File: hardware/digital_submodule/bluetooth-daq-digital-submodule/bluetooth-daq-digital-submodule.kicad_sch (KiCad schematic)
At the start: 163 parts, among them J1 MCU I/F, J2 Digital Inputs, J3 Digital Outputs, J4 Communication I/F, J5 RS-485 I/F, U1 74HC595, U2 74HC595, U3 74HC165, U4 74HC165, U5 24LC1025, U6 SN75176AD, U7 CD4053B, U8 CD4053B

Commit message: Addressed errors raised by KiCAD for digital sub-module.
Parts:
- added R200: 10k, symbol Device:R
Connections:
- net GND: now also R200.1
- net at U5.3 (A2): now also R200.2
- net 3V3 renamed +3V3
- net 5V renamed +5V

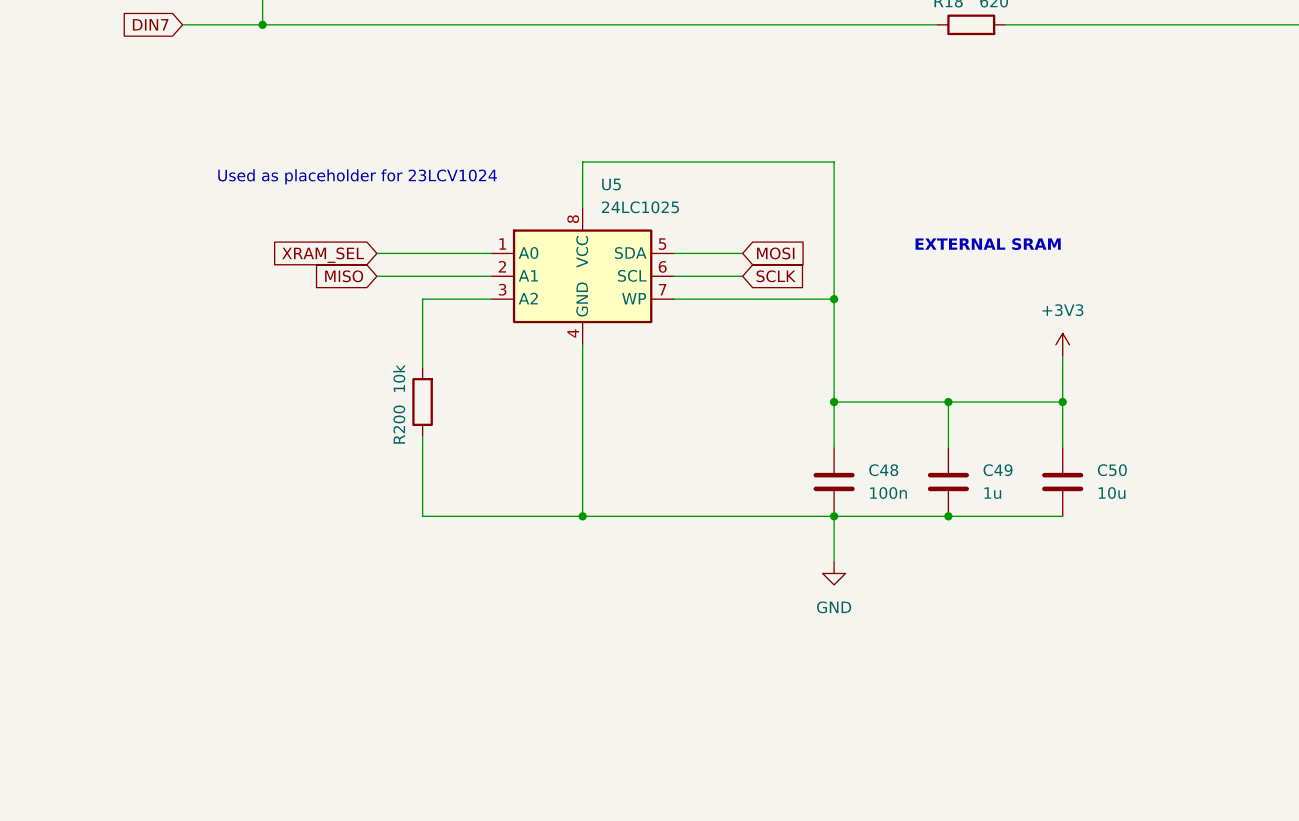
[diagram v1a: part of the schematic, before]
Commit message: Added footprints for components in digital_submodule
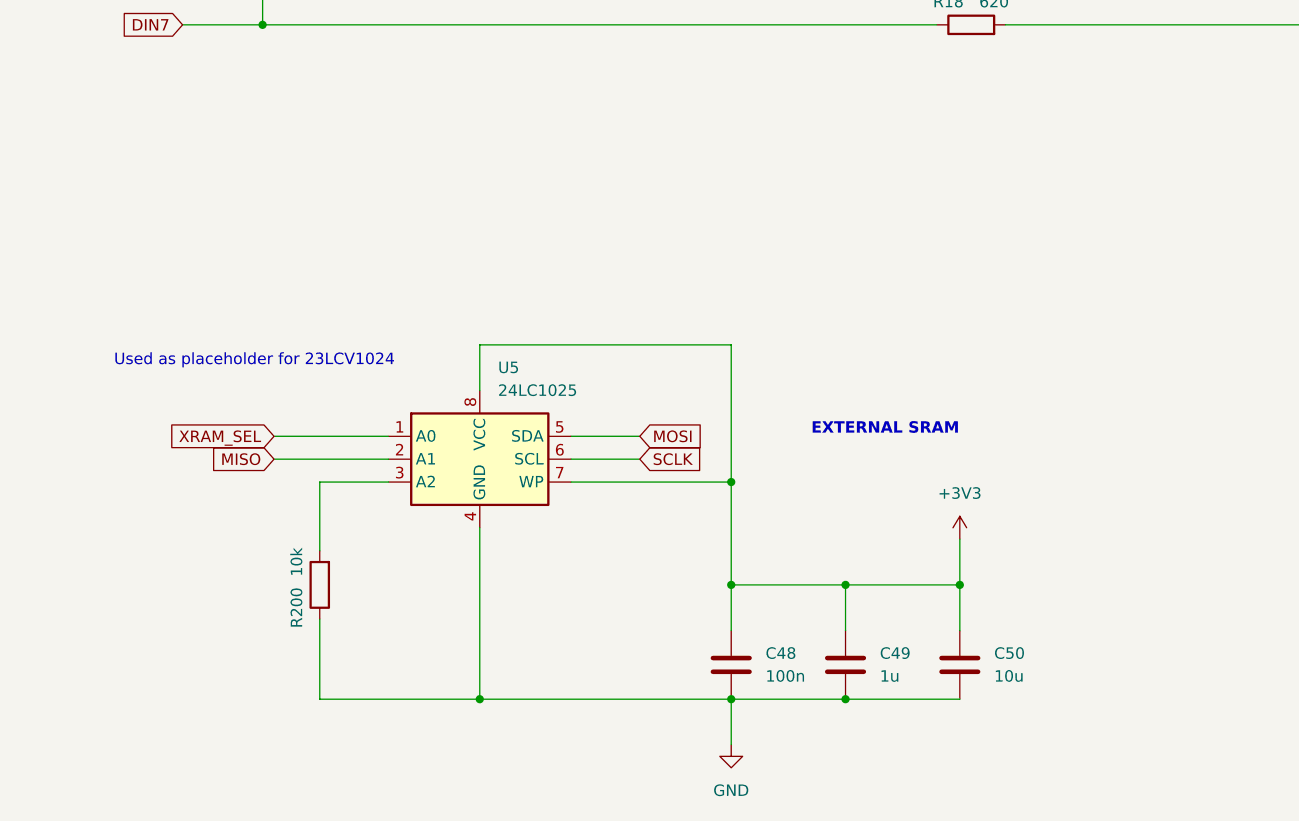
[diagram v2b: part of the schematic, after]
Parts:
- C1, C10, C11, C12, C13, C14, C15, C16, C17, C18, C19, C2, C20, C21, C22, C23, C24, C25, C29, C3, C30, C31, C32, C33, C34, C35, C36, C37, C38, C39, C4, C40, C41, C42, C43, C44, C45, C46, C47, C48, C49, C5, C50, C51, C52, C53, C54, C55, C56, C57, C6, C7, C8, C9: footprint (none) -> Capacitor_SMD:C_0805_2012Metric_Pad1.18x1.45mm_HandSolder
- D1, D10, D11, D12, D13, D14, D15, D16, D17, D18, D19, D2, D20, D21, D22, D23, D24, D25, D26, D27, D28, D29, D3, D30, D31, D32, D33, D34, D35, D36, D37, D38, D39, D4, D5, D6, D7, D8, D9: footprint (none) -> Diode_SMD:D_SMA_Handsoldering
- J1, J2, J3, J4: footprint (none) -> Connector_PinHeader_2.54mm:PinHeader_2x08_P2.54mm_Vertical
- J5: footprint (none) -> Connector_Phoenix_MC_HighVoltage:PhoenixContact_MCV_1,5_2-G-5.08_1x02_P5.08mm_Vertical
- R1, R10, R11, R12, R13, R14, R15, R16, R17, R18, R19, R2, R20, R200, R21, R22, R23, R24, R25, R26, R27, R28, R29, R3, R30, R31, R32, R33, R34, R35, R4, R41, R42, R43, R44, R45, R46, R47, R48, R49, R5, R50, R51, R52, R53, R54, R55, R56, R57, R58, R59, R6, R7, R8, R9: footprint (none) -> Resistor_SMD:R_0805_2012Metric_Pad1.20x1.40mm_HandSolder
- R38, R39, R40: footprint (none) -> Resistor_SMD:R_1206_3216Metric_Pad1.30x1.75mm_HandSolder
- U1, U2: footprint (none) -> Package_SO:SOIC-16_3.9x9.9mm_P1.27mm
- U3, U4: footprint (none) -> SN74HC165_custom:D16
- U5: footprint (none) -> 23LCV1024:SOIC8-N_MC_MCH
- U7, U8: footprint (none) -> CD4053BE_custom:D16
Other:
- moved on the sheet: C48, C49, C50, R200, U5

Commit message: Arranged components in PCB view according their functionality
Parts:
- removed D1, D10, D11, D12, D13, D14, D15, D16, D17, D18, D19, D2, D20, D21, D22, D23, D24, D25, D26, D27, D28, D29, D3, D30, D31, D32, D4, D5, D6, D7, D8, D9: SMAJ5.0CA, Diode_SMD:D_SMA_Handsoldering, symbol Device:D_TVS
- added DIP0, DIP1, DIP10, DIP11, DIP12, DIP13, DIP14, DIP15, DIP2, DIP3, DIP4, DIP5, DIP6, DIP7, DIP8, DIP9: D_Schottky, Diode_SMD:D_SMA_Handsoldering, symbol Device:D_Schottky
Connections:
- net GND: now also DIP0.2 (A), DIP1.2 (A), DIP10.2 (A), DIP11.2 (A), DIP12.2 (A), DIP13.2 (A), DIP14.2 (A), DIP15.2 (A), DIP2.2 (A), DIP3.2 (A), DIP4.2 (A), DIP5.2 (A), DIP6.2 (A), DIP7.2 (A), DIP8.2 (A), DIP9.2 (A)
- net at R23.2, U3.13 (D2): now also DIP2.1 (K)
- net at R21.2, U3.3 (D4): now also DIP4.1 (K)
- net at R34.2, U4.12 (D1): now also DIP9.1 (K)
- net at R18.2, U3.6 (D7): now also DIP7.1 (K)
- net at R22.2, U3.14 (D3): now also DIP3.1 (K)
- net at R25.2, U3.11 (D0): now also DIP0.1 (K)
- net at R24.2, U3.12 (D1): now also DIP1.1 (K)
- net at R20.2, U3.4 (D5): now also DIP5.1 (K)
- net at R19.2, U3.5 (D6): now also DIP6.1 (K)
- net at R33.2, U4.13 (D2): now also DIP10.1 (K)
- net at R30.2, U4.4 (D5): now also DIP13.1 (K)
- net at R35.2, U4.11 (D0): now also DIP8.1 (K)
- net at R28.2, U4.6 (D7): now also DIP15.1 (K)
- net at R32.2, U4.14 (D3): now also DIP11.1 (K)
- net at R29.2, U4.5 (D6): now also DIP14.1 (K)
- net at R31.2, U4.3 (D4): now also DIP12.1 (K)

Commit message: Decided on component arangement for digital input and digital output sections of the digital submodule.
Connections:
- net DIN0: no longer C29.2
- net DIN1: no longer C30.2
- net DIN10: no longer C45.2
- net DIN11: no longer C44.2
- net DIN12: no longer C43.2
- net DIN13: no longer C42.2
- net DIN14: no longer C41.2
- net DIN15: no longer C40.2
- net DIN2: no longer C31.2
- net DIN3: no longer C32.2
- net DIN4: no longer C33.2
- net DIN5: no longer C34.2
- net DIN6: no longer C35.2
- net DIN7: no longer C36.2
- net DIN8: no longer C47.2
- net DIN9: no longer C46.2
- net DOUT0: now also J3.15 (Pin_15); no longer J3.1 (Pin_1)
- net DOUT1: now also J3.13 (Pin_13); no longer J3.3 (Pin_3)
- net DOUT10: now also J3.12 (Pin_12); no longer J3.6 (Pin_6)
- net DOUT11: now also J3.10 (Pin_10); no longer J3.8 (Pin_8)
- net DOUT12: now also J3.8 (Pin_8); no longer J3.10 (Pin_10)
- net DOUT13: now also J3.6 (Pin_6); no longer J3.12 (Pin_12)
- net DOUT14: now also J3.4 (Pin_4); no longer J3.14 (Pin_14)
- net DOUT15: now also J3.2 (Pin_2); no longer J3.16 (Pin_16)
- net DOUT2: now also J3.11 (Pin_11); no longer J3.5 (Pin_5)
- net DOUT3: now also J3.9 (Pin_9); no longer J3.7 (Pin_7)
- net DOUT4: now also J3.7 (Pin_7); no longer J3.9 (Pin_9)
- net DOUT5: now also J3.5 (Pin_5); no longer J3.11 (Pin_11)
- net DOUT6: now also J3.3 (Pin_3); no longer J3.13 (Pin_13)
- net DOUT7: now also J3.1 (Pin_1); no longer J3.15 (Pin_15)
- net DOUT8: now also J3.16 (Pin_16); no longer J3.2 (Pin_2)
- net DOUT9: now also J3.14 (Pin_14); no longer J3.4 (Pin_4)
- net at DIP11.1 (K), R32.2, U4.14 (D3): now also C43.2
- net at DIP2.1 (K), R23.2, U3.13 (D2): now also C34.2
- net at DIP4.1 (K), R21.2, U3.3 (D4): now also C32.2
- net at DIP7.1 (K), R18.2, U3.6 (D7): now also C29.2
- net at DIP5.1 (K), R20.2, U3.4 (D5): now also C31.2
- net at DIP0.1 (K), R25.2, U3.11 (D0): now also C36.2
- net at DIP1.1 (K), R24.2, U3.12 (D1): now also C35.2
- net at DIP3.1 (K), R22.2, U3.14 (D3): now also C33.2
- net at DIP6.1 (K), R19.2, U3.5 (D6): now also C30.2
- net at DIP9.1 (K), R34.2, U4.12 (D1): now also C41.2
- net at DIP13.1 (K), R30.2, U4.4 (D5): now also C45.2
- net at DIP8.1 (K), R35.2, U4.11 (D0): now also C40.2
- net at DIP15.1 (K), R28.2, U4.6 (D7): now also C47.2
- net at DIP14.1 (K), R29.2, U4.5 (D6): now also C46.2
- net at DIP12.1 (K), R31.2, U4.3 (D4): now also C44.2
- net at DIP10.1 (K), R33.2, U4.13 (D2): now also C42.2
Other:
- moved on the sheet: C29, C30, C31, C32, C33, C34, C35, C36, C40, C41, C42, C43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

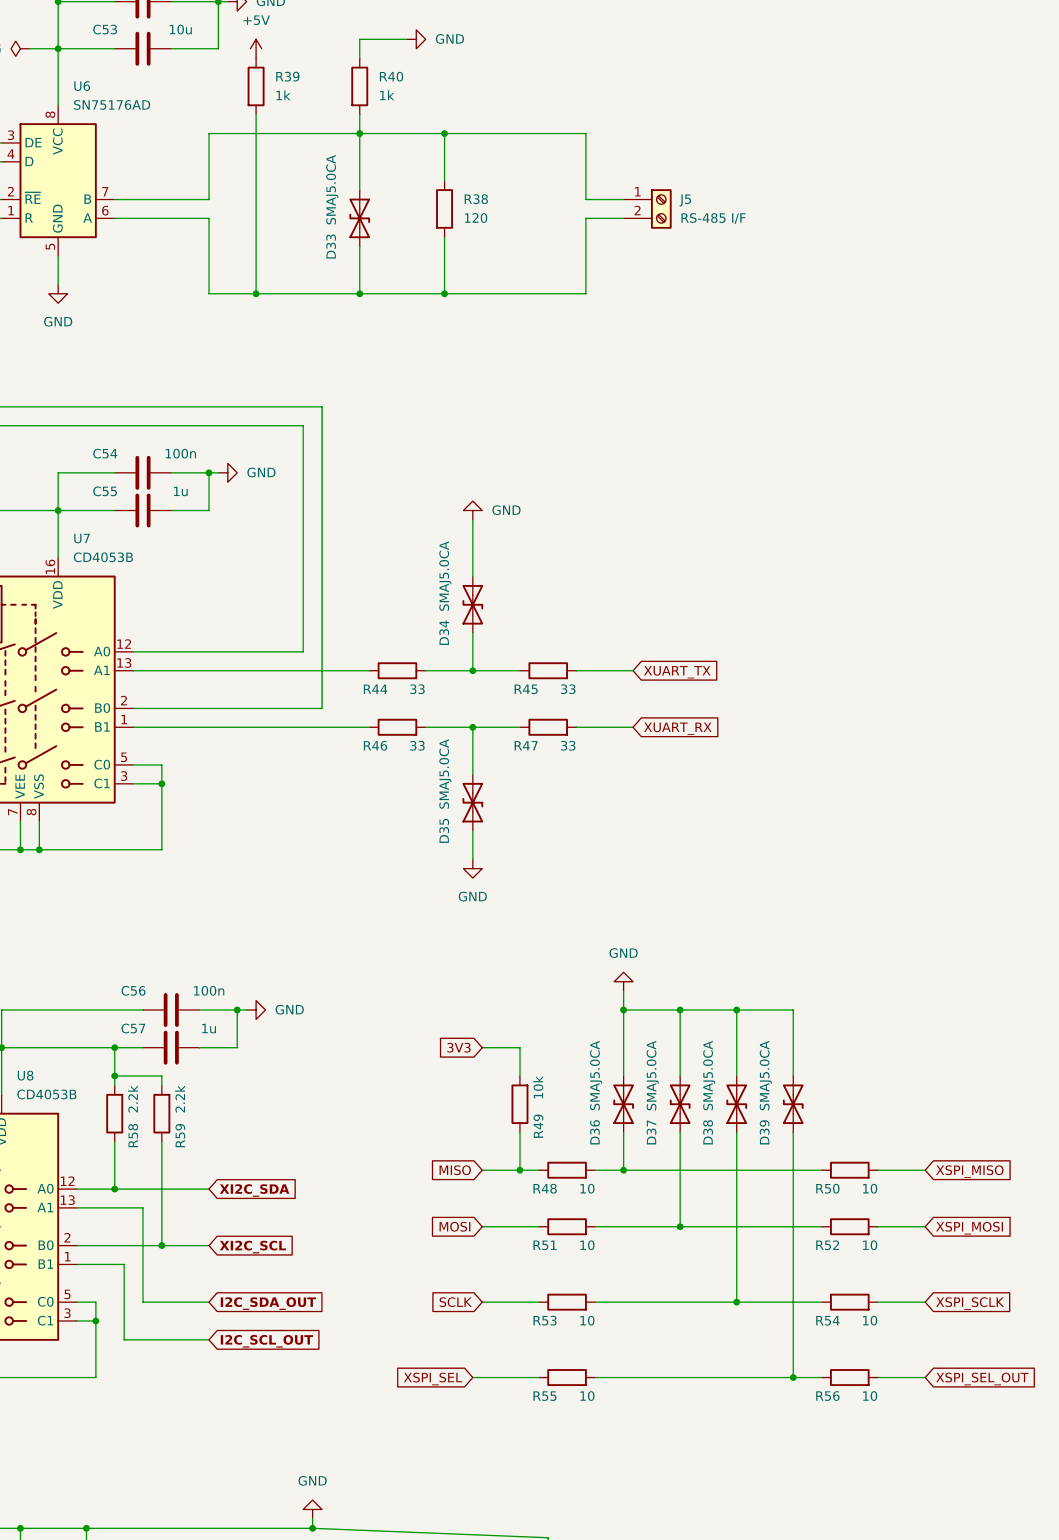
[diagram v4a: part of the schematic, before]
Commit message: Decided on initial component placement for digital submodule.
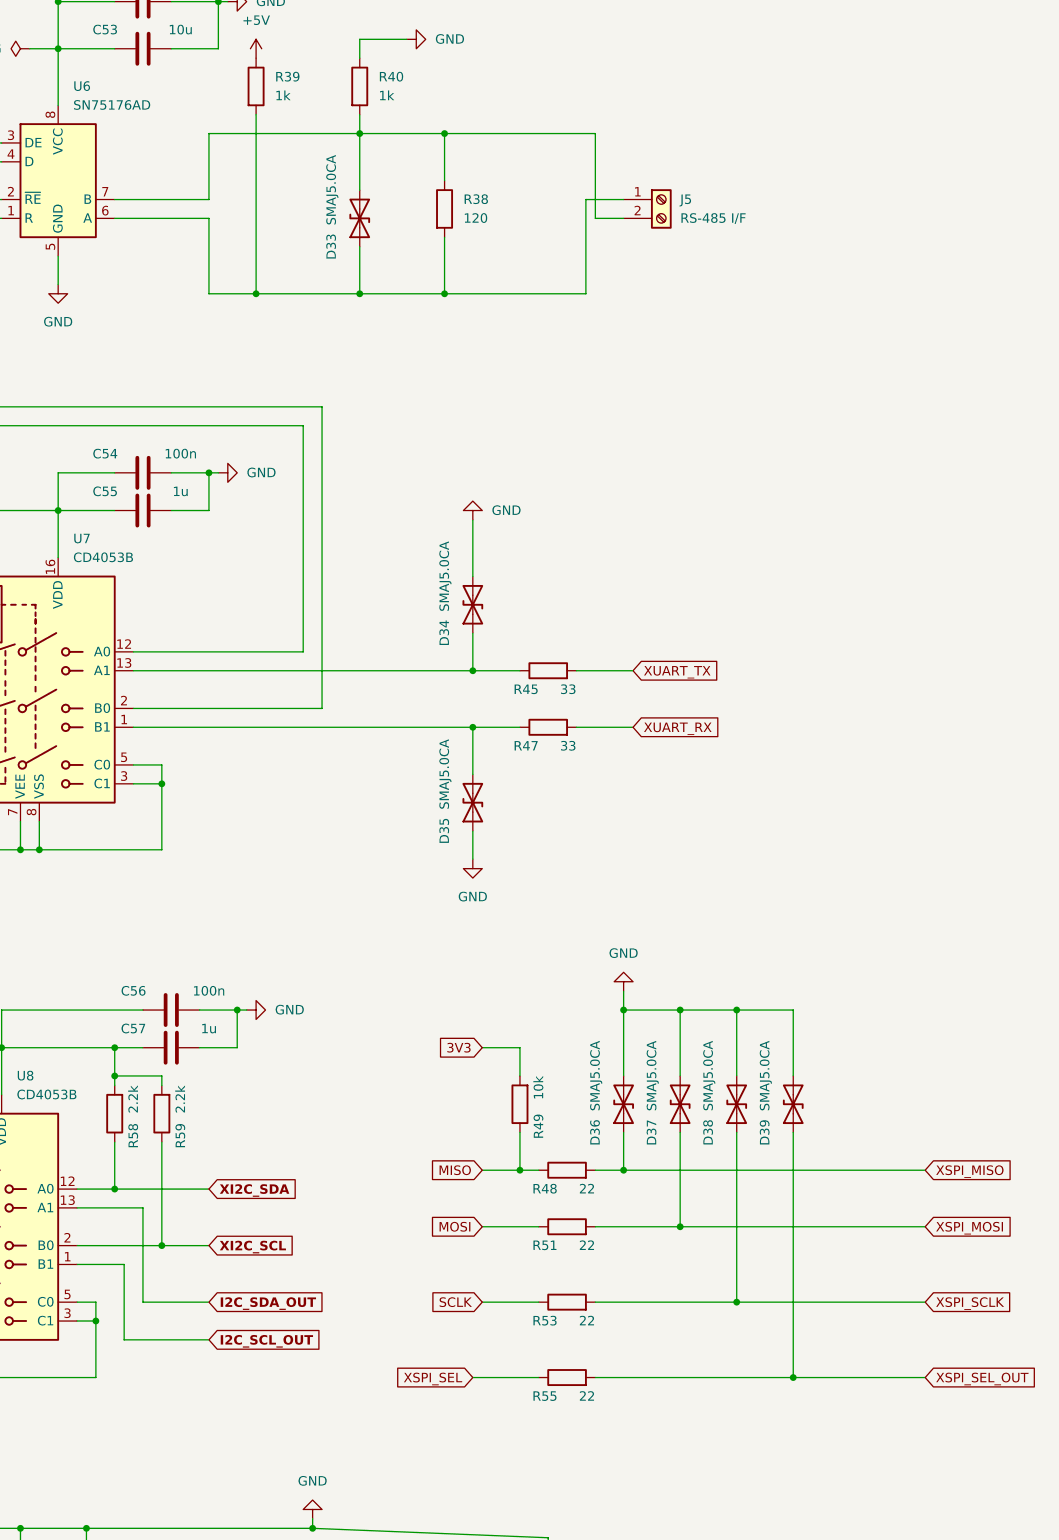
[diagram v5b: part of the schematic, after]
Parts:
- removed R44, R46: 33, Resistor_SMD:R_0805_2012Metric_Pad1.20x1.40mm_HandSolder, symbol Device:R
- removed R50, R52, R54, R56: 10, Resistor_SMD:R_0805_2012Metric_Pad1.20x1.40mm_HandSolder, symbol Device:R
- R48, R51, R53, R55: value 10 -> 22
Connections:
- net XSPI_MISO: now also D36.1 (A1), R48.2
- net XSPI_MOSI: now also D37.1 (A1), R51.2
- net XSPI_SCLK: now also D38.1 (A1), R53.2
- net XSPI_SEL_OUT: now also D39.1 (A1), R55.2
- net at D33.1 (A1), R38.2, R39.2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: now also J5.1 (Pin_1); no longer J5.2 (Pin_2)
- net at D33.2 (A2), R38.1, R40.2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: now also J5.2 (Pin_2); no longer J5.1 (Pin_1)
- net at D35.2 (A2), R47.1: now also U7.1 (B1)
- net at U7.13 (A1): now also D34.1 (A1), R45.1
